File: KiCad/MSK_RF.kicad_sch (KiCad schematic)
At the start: 69 parts, among them J3 Conn_01x12, J4 Conn_Coaxial, SW2 SW_Push, SW3 SW_Push, U1 STM32WLE5CCU6, U2 ADG918BRM, U3 TLV70233_SOT23-5, Y1 32.768 kHz, Y2 32MHz

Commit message: patch
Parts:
- removed Y2: 32MHz, symbol Device:Crystal_GND24
- added Y2: ECS-320-8-37-CKM-TR3, ECS320837CKMTR3, symbol SamacSys_Parts:ECS-320-8-37-CKM-TR3
- C10, C11, C12, C13, C14, C15, C16, C17, C18, C19, C20, C21, C22, C23, C24, C25, C26, C27, C28, C29, C3, C30, C31, C32, C4, C5, C6, C7, C8, C9: footprint (none) -> Capacitor_SMD:C_0603_1608Metric_Pad1.08x0.95mm_HandSolder
- D1: footprint (none) -> LED_SMD:LED_0603_1608Metric
- D6: footprint (none) -> LED_SMD:LED_0603_1608Metric_Pad1.05x0.95mm_HandSolder
- D7: value (none) -> Red LED; footprint (none) -> LED_SMD:LED_0603_1608Metric_Pad1.05x0.95mm_HandSolder
- J1: value (none) -> Conn_ARM_JTAG_SWD_10; footprint (none) -> Connector_PinSocket_2.54mm:PinSocket_2x05_P2.54mm_Vertical
- J2: value (none) -> Conn_01x12; footprint (none) -> Connector_PinSocket_2.54mm:PinSocket_1x12_P2.54mm_Vertical
- J4: footprint (none) -> Connector_Coaxial:SMA_Molex_73251-1153_EdgeMount_Horizontal
- J5: value (none) -> USB_B_Micro; footprint (none) -> SamacSys_Parts:47346-0001
- JP1, JP2, JP3: footprint (none) -> Connector_PinHeader_2.54mm:PinHeader_1x02_P2.54mm_Vertical
- L1, L2, L4, L5, L6: footprint (none) -> Inductor_SMD:L_0603_1608Metric_Pad1.05x0.95mm_HandSolder
- R1, R9: value (none) -> 10K; footprint (none) -> Resistor_SMD:R_0603_1608Metric_Pad0.98x0.95mm_HandSolder
- R10, R2, R3, R4, R5, R6, R7, R8: footprint (none) -> Resistor_SMD:R_0603_1608Metric_Pad0.98x0.95mm_HandSolder
- SW1: value (none) -> SW_Push; footprint (none) -> SamacSys_Parts:FSM2J_1
- Y1: footprint Oscillator:Oscillator_SMD_Abracon_ASDMB-4Pin_2.5x2.0mm -> SamacSys_Parts:ECX-31B
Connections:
- net 3.3V: now also C5.1; no longer C5.2
- net GND: now also C5.2, Y2.2 (GND_1), Y2.4 (GND_2); no longer C5.1, U1.26 (OSC_IN), U1.27 (OSC_OUT)
- new net: U1.27 (OSC_OUT), Y2.1 (IN/OUT)
- new net: U1.26 (OSC_IN), Y2.3 (OUT/IN)
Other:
- moved on the sheet: C5

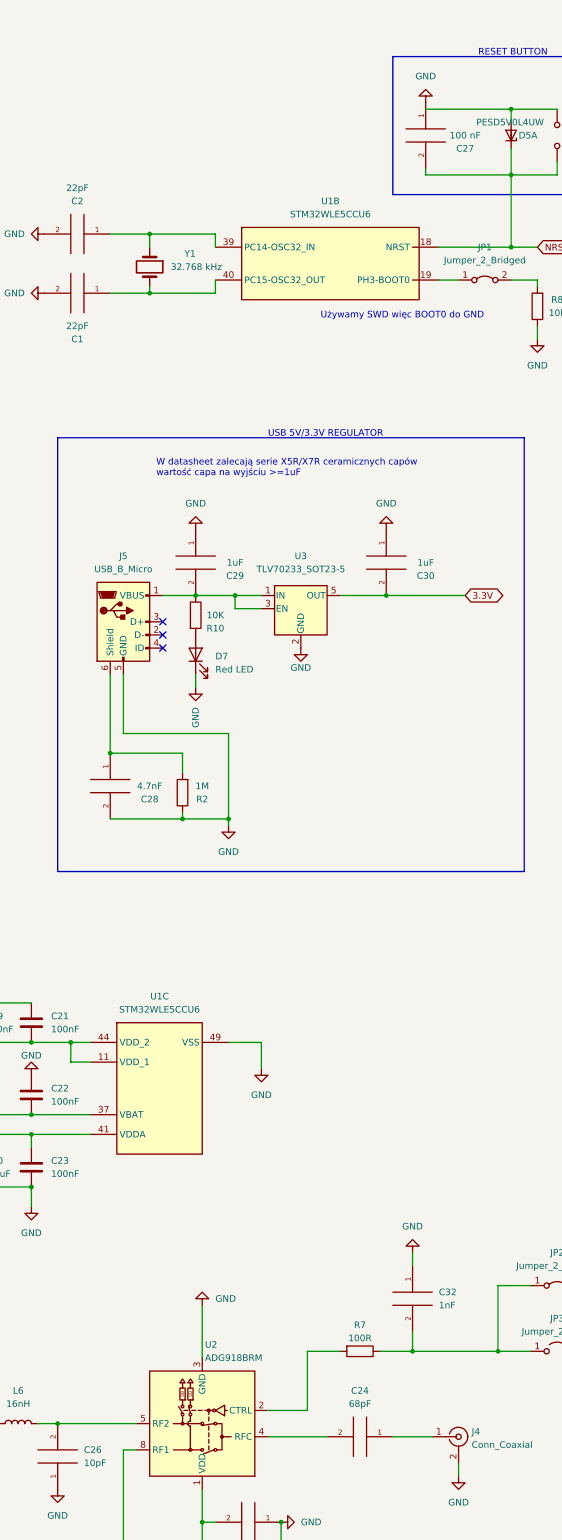
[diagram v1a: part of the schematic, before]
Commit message: Added i2c header
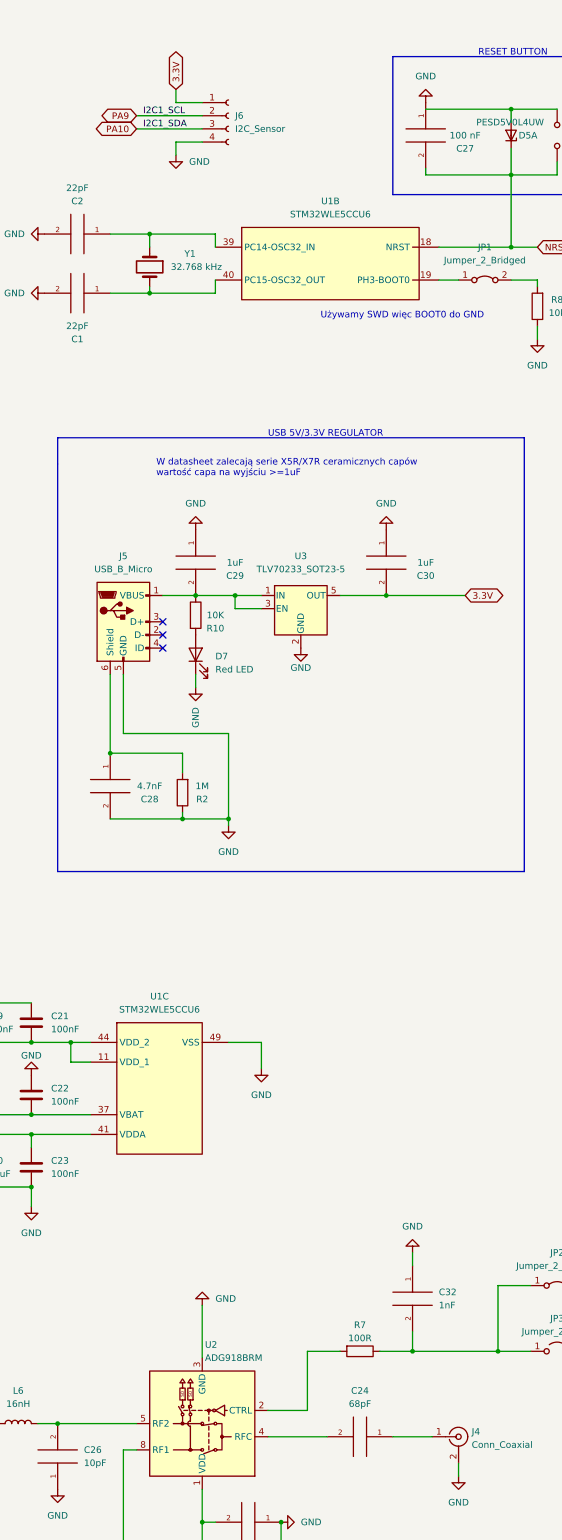
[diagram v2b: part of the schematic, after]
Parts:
- added J6: I2C_Sensor, Connector_PinHeader_2.54mm:PinHeader_1x04_P2.54mm_Vertical, symbol Connector:Conn_01x04_Female
- Y2: footprint ECS320837CKMTR3 -> SamacSys_Parts:ECS320837CKMTR3
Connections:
- net 3.3V: now also J6.1 (Pin_1)
- net GND: now also J6.4 (Pin_4)
- net PA10: now also J6.3 (Pin_3)
- net PA9: now also J6.2 (Pin_2)

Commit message: pcb update
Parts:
- removed C28: 4.7nF, Capacitor_SMD:C_0603_1608Metric_Pad1.08x0.95mm_HandSolder, symbol pspice:CAP
- removed D3, D4, D5: PESD5V0L4UW, Package_TO_SOT_SMD:SOT-665, symbol Power_Protection:PESD5V0L4UW
- removed J1: Conn_ARM_JTAG_SWD_10, Connector_PinSocket_2.54mm:PinSocket_2x05_P2.54mm_Vertical, symbol Connector:Conn_ARM_JTAG_SWD_10
- removed J5: USB_B_Micro, SamacSys_Parts:47346-0001, symbol Connector:USB_B_Micro
- removed R2: 1M, Resistor_SMD:R_0603_1608Metric_Pad0.98x0.95mm_HandSolder, symbol Device:R
- removed SW1, SW2, SW3: SW_Push, SamacSys_Parts:FSM2J_1, symbol Switch:SW_Push
- added D2, D3, D4: ESDALC6V1-1U2, ESDALC6V11U2, symbol SamacSys_Parts:ESDALC6V1-1U2
- added J1: SWD connector, Connector_PinHeader_2.54mm:PinHeader_1x04_P2.54mm_Vertical, symbol Connector:Conn_01x04_Female
- added J5: (no value), symbol SamacSys_Parts:47346-0001
- added R11, R12, R13, R14: 0, SamacSys_Parts:transition, symbol Device:R
- added S1, S2, S3: Button FSM2JSMAATR, FSM2J_1, symbol SamacSys_Parts:FSM2JSMAATR
- D1: footprint LED_SMD:LED_0603_1608Metric -> LED_SMD:LED_0603_1608Metric_Pad1.05x0.95mm_HandSolder
- U1: value STM32WLE5CCU6 -> (none); footprint SamacSys_Parts:QFN50P700X700X60-49N-D -> (none)
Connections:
- net 3.3V: now also J1.1 (Pin_1)
- net GND: now also C13.2, C25.2, D2.2, D3.2, D4.2, J1.4 (Pin_4), J5.5 (GND), S1.3, S1.4, S2.3, S2.4, S3.1, S3.2; no longer C13.1, C25.1
- net NRST: now also D4.1, S3.3, S3.4
- net PA13: now also J1.3 (Pin_3)
- net PA14: now also J1.2 (Pin_2)
- net at C24.2: now also R14.2; no longer U2.4 (RFC)
- net at C14.2, L4.2, L5.1: now also R11.2; no longer U1.23 (RFO_HP)
- net at C26.2, L6.2: now also R13.2; no longer U2.5 (RF2)
- net at C29.2, R10.1, U3.1 (IN)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: now also J5.1 (VBUS)
- net at R4.2: now also C25.1, D3.1, S2.1, S2.2
- net at C11.2: now also R12.2; no longer U2.8 (RF1)
- net at R3.2: now also C13.1, D2.1, S1.1, S1.2
- new net: R11.1, U1.23 (RFO_HP)
- new net: R13.1, U2.5 (RF2)
- new net: R12.1, U2.8 (RF1)
- new net: R14.1, U2.4 (RFC)
- no-connect marks 10 -> 8
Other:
- note added: "VDD dla switcha to 2.75V, sam switch bierze <1uA to dałem zwykły dzielnik napięcia z 3.3V na 2.75V"
- note removed: "SWD CONNECTOR"
- note removed: "VDD dla switcha to 2.75V, sam switch bierzę <1uA to dałem zwykły dzielnik napięcia z 3.3V na 2.75V"
- moved on the sheet: C25, C27, J6, R4

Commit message: almost finished pcb
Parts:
- removed J1: SWD connector, Connector_PinHeader_2.54mm:PinHeader_1x04_P2.54mm_Vertical, symbol Connector:Conn_01x04_Female
- removed J6: I2C_Sensor, Connector_PinHeader_2.54mm:PinHeader_1x04_P2.54mm_Vertical, symbol Connector:Conn_01x04_Female
- removed JP2: Jumper_2_Bridged, Connector_PinHeader_2.54mm:PinHeader_1x02_P2.54mm_Vertical, symbol Jumper:Jumper_2_Bridged
- removed JP3: Jumper_2_Open, Connector_PinHeader_2.54mm:PinHeader_1x02_P2.54mm_Vertical, symbol Jumper:Jumper_2_Open
- removed R11, R12, R13, R14: 0, SamacSys_Parts:transition, symbol Device:R
- J5: value (none) -> 47346-0001; footprint (none) -> 47346-0001
- U1: value (none) -> STM32WLE5CCU6; footprint (none) -> SamacSys_Parts:QFN50P700X700X60-49N-D
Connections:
- net 3.3V: now also J3.4 (Pin_4)
- net FE_CTRL: now also C32.2, R7.1
- net GND: no longer J3.4 (Pin_4)
- net at C24.2: now also U2.4 (RFC)
- net at U1.23 (RFO_HP): now also C14.2, L4.2, L5.1
- net at C26.2, L6.2: now also U2.5 (RF2)
- net at C11.2: now also U2.8 (RF1)

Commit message: pcb update
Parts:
- added J1: (no value), symbol Connector:Conn_01x05_Male
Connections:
- net 3.3V: now also J1.1 (Pin_1)
- net GND: now also J1.5 (Pin_5)
- net NRST: now also J1.4 (Pin_4)
- net PA13: now also J1.2 (Pin_2)
- net PA14: now also J1.3 (Pin_3)
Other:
- note added: "SWD conn"
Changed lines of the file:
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@@
     (stroke (width 0) (type default) (color 0 0 0 0))
   )
+  (wire (pts (xy 149.86 102.87) (xy 163.83 102.87))
+    (stroke (width 0) (type default) (color 0 0 0 0))
+  )
   (wire (pts (xy 127 73.66) (xy 140.97 73.66))
     (stroke (width 0) (type default) (color 0 0 0 0))
@@
     (stroke (width 0) (type default) (color 0 0 0 0))
   )
+  (wire (pts (xy 163.83 97.79) (xy 149.86 97.79))
+    (stroke (width 0) (type default) (color 0 0 0 0))
+  )
   (wire (pts (xy 99.06 294.64) (xy 66.04 294.64))
     (stroke (width 0) (type default) (color 0 0 0 0))
@@
     (stroke (width 0) (type default) (color 0 0 0 0))
   )
+  (wire (pts (xy 149.86 95.25) (xy 163.83 95.25))
+    (stroke (width 0) (type default) (color 0 0 0 0))
+  )
   (wire (pts (xy 33.02 41.91) (xy 45.72 41.91))
     (stroke (width 0) (type default) (color 0 0 0 0))
   )
+  (wire (pts (xy 163.83 100.33) (xy 149.86 100.33))
+    (stroke (width 0) (type default) (color 0 0 0 0))
+  )
   (wire (pts (xy 132.08 293.37) (xy 163.83 293.37))
     (stroke (width 0) (type default) (color 0 0 0 0))
@@
     (stroke (width 0) (type default) (color 0 0 0 0))
   )
+  (wire (pts (xy 149.86 105.41) (xy 163.83 105.41))
+    (stroke (width 0) (type default) (color 0 0 0 0))
+  )
   (wire (pts (xy 307.34 26.67) (xy 307.34 31.75))
     (stroke (width 0) (type default) (color 0 0 0 0))
@@
     (effects (font (size 1.27 1.27)) (justify left bottom))
   )
+  (text "SWD conn" (at 151.13 90.17 0)
+    (effects (font (size 1.27 1.27)) (justify left bottom))
+  )
   (text "USER BUTTON 2\n" (at 62.23 170.18 0)
     (effects (font (size 1.27 1.27)) (justify left bottom))
@@
     (effects (font (size 1.27 1.27)) (justify left bottom))
   )
+  (label "SWCLK" (at 162.56 100.33 180)
+    (effects (font (size 1.27 1.27)) (justify right bottom))
+  )
   (label "SWCLK" (at 34.29 64.77 0)
     (effects (font (size 1.27 1.27)) (justify left bottom))
@@
     (effects (font (size 1.27 1.27)) (justify left bottom))
   )
+  (label "SWDIO" (at 162.56 97.79 180)
+    (effects (font (size 1.27 1.27)) (justify right bottom))
+  )
   (label "SPI1_MOSI" (at 163.83 50.8 0)
     (effects (font (size 1.27 1.27)) (justify left bottom))
@@
     )
   )
+  (global_label "PA13" (shape bidirectional) (at 163.83 97.79 0) (fields_autoplaced)
+    (effects (font (size 1.27 1.27)) (justify left))
+    (property "Intersheet References" "${INTERSHEET_REFS}" (id 0) (at 171.0207 97.7106 0)
+      (effects (font (size 1.27 1.27)) (justify left) hide)
+    )
+  )
+  (global_label "PA14" (shape bidirectional) (at 163.83 100.33 0) (fields_autoplaced)
+    (effects (font (size 1.27 1.27)) (justify left))
+    (property "Intersheet References" "${INTERSHEET_REFS}" (id 0) (at 171.0207 100.4094 0)
+      (effects (font (size 1.27 1.27)) (justify left) hide)
+    )
+  )
+  (global_label "GND" (shape bidirectional) (at 163.83 105.41 0) (fields_autoplaced)
+    (effects (font (size 1.27 1.27)) (justify left))
+    (property "Intersheet References" "${INTERSHEET_REFS}" (id 0) (at 170.1136 105.4894 0)
+      (effects (font (size 1.27 1.27)) (justify left) hide)
+    )
+  )
   (global_label "PA14" (shape bidirectional) (at 127 76.2 180) (fields_autoplaced)
     (effects (font (size 1.27 1.27)) (justify right))
@@
     )
   )
+  (global_label "NRST" (shape bidirectional) (at 163.83 102.87 0) (fields_autoplaced)
+    (effects (font (size 1.27 1.27)) (justify left))
+    (property "Intersheet References" "${INTERSHEET_REFS}" (id 0) (at 171.0207 102.7906 0)
+      (effects (font (size 1.27 1.27)) (justify left) hide)
+    )
+  )
   (global_label "PA11" (shape bidirectional) (at 33.02 57.15 180) (fields_autoplaced)
     (effects (font (size 1.27 1.27)) (justify right))
@@
     )
   )
+  (global_label "3.3V" (shape bidirectional) (at 163.83 95.25 0) (fields_autoplaced)
+    (effects (font (size 1.27 1.27)) (justify left))
+    (property "Intersheet References" "${INTERSHEET_REFS}" (id 0) (at 170.3555 95.1706 0)
+      (effects (font (size 1.27 1.27)) (justify left) hide)
+    )
+  )
   (global_label "PA5" (shape bidirectional) (at 33.02 41.91 180) (fields_autoplaced)
     (effects (font (size 1.27 1.27)) (justify right))
@@
     (pin "1")
   )
+  (symbol (lib_id "Connector:Conn_01x05_Male") (at 144.78 100.33 0) (unit 1)
+    (in_bom yes) (on_board yes) (fields_autoplaced)
+    (property "Reference" "J1" (id 0) (at 145.415 90.17 0))
+    (property "Value" "" (id 1) (at 145.415 92.71 0))
+    (property "Footprint" "" (id 2) (at 144.78 100.33 0)
+      (effects (font (size 1.27 1.27)) hide)
+    )
+    (property "Datasheet" "~" (id 3) (at 144.78 100.33 0)
+      (effects (font (size 1.27 1.27)) hide)
+    )
+    (pin "1")
+    (pin "2")
+    (pin "3")
+    (pin "4")
+    (pin "5")
+  )
   (symbol (lib_id "power:GND") (at 77.47 261.62 0) (unit 1)
     (in_bom yes) (on_board yes) (fields_autoplaced)
@@
       (reference "D7") (unit 1) (value "Red LED") (footprint "LED_SMD:LED_0603_1608Metric_Pad1.05x0.95mm_HandSolder")
     )
+    (path "/c9d8cfeb-d425-42c9-ab0f-f723079d665e"
+      (reference "J1") (unit 1) (value "Conn_01x05_Male") (footprint "Connector_PinHeader_2.54mm:PinHeader_1x05_P2.54mm_Vertical")
+    )
     (path "/b0c5276f-f289-4a2c-9232-968f6225c06d"

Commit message: finished pcb
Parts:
- J1: value (none) -> Conn_01x05_Male; footprint (none) -> Connector_PinHeader_2.54mm:PinHeader_1x05_P2.54mm_Vertical
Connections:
- net 3.3V: now also J3.1 (Pin_1); no longer J3.4 (Pin_4)
- net GND: no longer J3.5 (Pin_5), U1.14 (PA6), U1.32 (PB12)
- new net PA6: J3.5 (Pin_5), U1.14 (PA6)
- new net PB12: J3.4 (Pin_4), U1.32 (PB12)
- no-connect marks 8 -> 7
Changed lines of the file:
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@@
   (junction (at 201.93 237.49) (diameter 0) (color 0 0 0 0)
   )
-  (no_connect (at 163.83 76.2))
   (no_connect (at 240.03 135.89))
   (no_connect (at 132.08 298.45))
@@
     (stroke (width 0) (type default) (color 0 0 0 0))
   )
+  (wire (pts (xy 163.83 76.2) (xy 177.8 76.2))
+    (stroke (width 0) (type default) (color 0 0 0 0))
+  )
   (wire (pts (xy 267.97 279.4) (xy 274.32 279.4))
     (stroke (width 0) (type default) (color 0 0 0 0))
@@
     (effects (font (size 1.27 1.27)) (justify left bottom))
   )
-  (label "LPUART1_CTS" (at 163.83 63.5 0)
-    (effects (font (size 1.27 1.27)) (justify left bottom))
-  )
   (label "SWCLK" (at 162.56 100.33 180)
     (effects (font (size 1.27 1.27)) (justify right bottom))
@@
     (effects (font (size 1.27 1.27)) (justify left bottom))
   )
-  (label "LPUART_RTS" (at 163.83 66.04 0)
-    (effects (font (size 1.27 1.27)) (justify left bottom))
-  )
   (label "SWDIO" (at 162.56 97.79 180)
     (effects (font (size 1.27 1.27)) (justify right bottom))
@@
     (effects (font (size 1.27 1.27)) (justify left bottom))
   )
+  (label "LPUART1_CTS" (at 163.83 66.04 0)
+    (effects (font (size 1.27 1.27)) (justify left bottom))
+  )
   (label "SPI1_MOSI" (at 34.29 46.99 0)
     (effects (font (size 1.27 1.27)) (justify left bottom))
@@
     (effects (font (size 1.27 1.27)) (justify left bottom))
   )
+  (label "LPUART_RTS" (at 163.83 68.58 0)
+    (effects (font (size 1.27 1.27)) (justify left bottom))
+  )
   (global_label "PA0" (shape bidirectional) (at 33.02 29.21 180) (fields_autoplaced)
     (effects (font (size 1.27 1.27)) (justify right))
@@
     )
   )
-  (global_label "3.3V" (shape bidirectional) (at 177.8 68.58 0) (fields_autoplaced)
-    (effects (font (size 1.27 1.27)) (justify left))
-    (property "Intersheet References" "${INTERSHEET_REFS}" (id 0) (at 184.3255 68.5006 0)
+  (global_label "PB12" (shape bidirectional) (at 177.8 68.58 0) (fields_autoplaced)
+    (effects (font (size 1.27 1.27)) (justify left))
+    (property "Intersheet References" "${INTERSHEET_REFS}" (id 0) (at 185.1721 68.5006 0)
       (effects (font (size 1.27 1.27)) (justify left) hide)
     )
@@
     (effects (font (size 1.27 1.27)) (justify left))
     (property "Intersheet References" "${INTERSHEET_REFS}" (id 0) (at 336.5441 279.3206 0)
+      (effects (font (size 1.27 1.27)) (justify left) hide)
+    )
+  )
+  (global_label "3.3V" (shape bidirectional) (at 177.8 76.2 0) (fields_autoplaced)
+    (effects (font (size 1.27 1.27)) (justify left))
+    (property "Intersheet References" "${INTERSHEET_REFS}" (id 0) (at 184.3255 76.1206 0)
       (effects (font (size 1.27 1.27)) (justify left) hide)
     )
@@
     (in_bom yes) (on_board yes) (fields_autoplaced)
     (property "Reference" "J1" (id 0) (at 145.415 90.17 0))
-    (property "Value" "" (id 1) (at 145.415 92.71 0))
-    (property "Footprint" "" (id 2) (at 144.78 100.33 0)
-      (effects (font (size 1.27 1.27)) hide)
-    )
+    (property "Value" "Conn_01x05_Male" (id 1) (at 145.415 92.71 0))
+    (property "Footprint" "Connector_PinHeader_2.54mm:PinHeader_1x05_P2.54mm_Vertical" (id 2) (at 144.78 100.33 0)
+      (effects (font (size 1.27 1.27)) hide)
+    )
